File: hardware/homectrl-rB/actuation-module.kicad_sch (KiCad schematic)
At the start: 26 parts, among them J6 PUMP0-CONN, J7 PUMP1-CONN, J8 STEP-CONN, Q2 AO3400A, Q3 AO3400A, U8 TMC2209

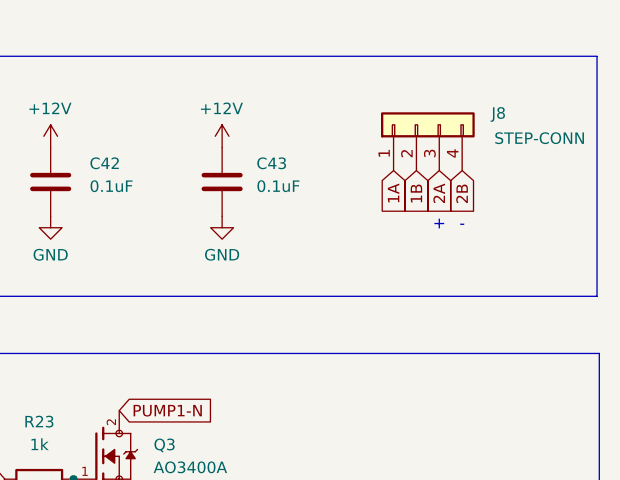
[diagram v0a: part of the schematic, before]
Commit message: connector fixes
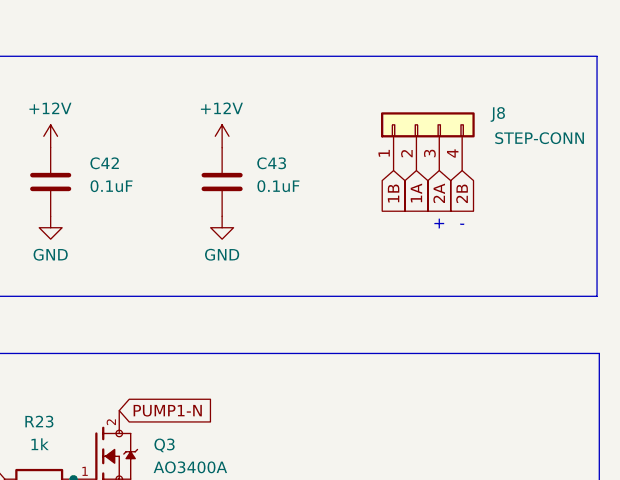
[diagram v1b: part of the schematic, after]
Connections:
- net 1A: now also J8.2 (Pin_2); no longer J8.1 (Pin_1)
- net 1B: now also J8.1 (Pin_1); no longer J8.2 (Pin_2)
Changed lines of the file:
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@@
+		)
+	)
+	(global_label "PGATE-1"
+		(shape input)
+		(at 161.29 67.31 180)
+		(fields_autoplaced yes)
+		(effects
+			(font
+				(size 1.27 1.27)
+			)
+			(justify right)
+		)
+		(property "Intersheetrefs" "${INTERSHEET_REFS}"
+			(at 149.7777 67.31 0)
+			(effects
+				(font
+					(size 1.27 1.27)
+				)
+				(justify right)
+				(hide yes)
+			)
+		)
+	)
+	(global_label "1A"
+		(shape input)
+		(at 207.01 33.02 270)
+		(fields_autoplaced yes)
+		(effects
+			(font
+				(size 1.27 1.27)
+			)
+			(justify right)
+		)
+		(property "Intersheetrefs" "${INTERSHEET_REFS}"
+			(at 207.01 38.3033 90)
+			(effects
+				(font
+					(size 1.27 1.27)
+				)
+				(justify right)
+				(hide yes)
+			)
+		)
+	)
+	(global_label "2B"
+		(shape input)
+		(at 118.11 105.41 90)
+		(fields_autoplaced yes)
+		(effects
+			(font
+				(size 1.27 1.27)
+			)
+			(justify left)
+		)
+		(property "Intersheetrefs" "${INTERSHEET_REFS}"
+			(at 118.11 99.9453 90)
+			(effects
+				(font
+					(size 1.27 1.27)
+				)
+				(justify left)
+				(hide yes)
+			)
+		)
+	)
+	(global_label "2A"
+		(shape input)
+		(at 209.55 33.02 270)
+		(fields_autoplaced yes)
+		(effects
+			(font
+				(size 1.27 1.27)
+			)
+			(justify right)
+		)
+		(property "Intersheetrefs" "${INTERSHEET_REFS}"
+			(at 209.55 38.3033 90)
+			(effects
+				(font
+					(size 1.27 1.27)
+				)
+				(justify right)
+				(hide yes)
+			)
+		)
+	)
+	(global_label "PUMP0-N"
+		(shape input)
+		(at 129.54 59.69 0)
+		(fields_autoplaced yes)
+		(effects
+			(font
+				(size 1.27 1.27)
+			)
+			(justify left)
+		)
+		(property "Intersheetrefs" "${INTERSHEET_REFS}"
+			(at 141.9595 59.69 0)
+			(effects
+				(font
+					(size 1.27 1.27)
+				)
+				(justify left)
+				(hide yes)
+			)
+		)
+	)
+	(global_label "S3-TX"
+		(shape input)
+		(at 118.11 146.05 270)
+		(fields_autoplaced yes)
+		(effects
+			(font
+				(size 1.27 1.27)
+			)
+			(justify right)
+		)
+		(property "Intersheetrefs" "${INTERSHEET_REFS}"
+			(at 118.11 155.2037 90)
+			(effects
+				(font
+					(size 1.27 1.27)
+				)
+				(justify right)
+				(hide yes)
+			)
+		)
+	)
+	(global_label "PUMP1-N"
+		(shape input)
+		(at 173.99 59.69 0)
+		(fields_autoplaced yes)
+		(effects
+			(font
+				(size 1.27 1.27)
+			)
+			(justify left)
+		)
+		(property "Intersheetrefs" "${INTERSHEET_REFS}"
+			(at 186.4095 59.69 0)
+			(effects
+				(font
+					(size 1.27 1.27)
+				)
+				(justify left)
+				(hide yes)
+			)
 		)
 	)
 	(global_label "1B"
 		(shape input)
-		(at 207.01 33.02 270)
-		(fields_autoplaced yes)
-		(effects
-			(font
-				(size 1.27 1.27)
-			)
-			(justify right)
-		)
-		(property "Intersheetrefs" "${INTERSHEET_REFS}"
-			(at 207.01 38.4847 90)
-			(effects
-				(font
-					(size 1.27 1.27)
-				)
-				(justify right)
-				(hide yes)
-			)
-		)
-	)
-	(global_label "PGATE-1"
-		(shape input)
-		(at 161.29 67.31 180)
-		(fields_autoplaced yes)
-		(effects
-			(font
-				(size 1.27 1.27)
-			)
-			(justify right)
-		)
-		(property "Intersheetrefs" "${INTERSHEET_REFS}"
-			(at 149.7777 67.31 0)
-			(effects
-				(font
-					(size 1.27 1.27)
-				)
-				(justify right)
-				(hide yes)
-			)
-		)
-	)
-	(global_label "2B"
-		(shape input)
-		(at 118.11 105.41 90)
-		(fields_autoplaced yes)
-		(effects
-			(font
-				(size 1.27 1.27)
-			)
-			(justify left)
-		)
-		(property "Intersheetrefs" "${INTERSHEET_REFS}"
-			(at 118.11 99.9453 90)
-			(effects
-				(font
-					(size 1.27 1.27)
-				)
-				(justify left)
-				(hide yes)
-			)
-		)
-	)
-	(global_label "2A"
-		(shape input)
-		(at 209.55 33.02 270)
-		(fields_autoplaced yes)
-		(effects
-			(font
-				(size 1.27 1.27)
-			)
-			(justify right)
-		)
-		(property "Intersheetrefs" "${INTERSHEET_REFS}"
-			(at 209.55 38.3033 90)
-			(effects
-				(font
-					(size 1.27 1.27)
-				)
-				(justify right)
-				(hide yes)
-			)
-		)
-	)
-	(global_label "PUMP0-N"
-		(shape input)
-		(at 129.54 59.69 0)
-		(fields_autoplaced yes)
-		(effects
-			(font
-				(size 1.27 1.27)
-			)
-			(justify left)
-		)
-		(property "Intersheetrefs" "${INTERSHEET_REFS}"
-			(at 141.9595 59.69 0)
-			(effects
-				(font
-					(size 1.27 1.27)
-				)
-				(justify left)
-				(hide yes)
-			)
-		)
-	)
-	(global_label "S3-TX"
-		(shape input)
-		(at 118.11 146.05 270)
-		(fields_autoplaced yes)
-		(effects
-			(font
-				(size 1.27 1.27)
-			)
-			(justify right)
-		)
-		(property "Intersheetrefs" "${INTERSHEET_REFS}"
-			(at 118.11 155.2037 90)
-			(effects
-				(font
-					(size 1.27 1.27)
-				)
-				(justify right)
-				(hide yes)
-			)
-		)
-	)
-	(global_label "PUMP1-N"
-		(shape input)
-		(at 173.99 59.69 0)
-		(fields_autoplaced yes)
-		(effects
-			(font
-				(size 1.27 1.27)
-			)
-			(justify left)
-		)
-		(property "Intersheetrefs" "${INTERSHEET_REFS}"
-			(at 186.4095 59.69 0)
+		(at 168.91 113.03 0)
+		(fields_autoplaced yes)
+		(effects
+			(font
+				(size 1.27 1.27)
+			)
+			(justify left)
+		)
+		(property "Intersheetrefs" "${INTERSHEET_REFS}"
+			(at 174.3747 113.03 0)
 			(effects
 				(font
@@
 	(global_label "1A"
 		(shape input)
+		(at 168.91 118.11 0)
+		(fields_autoplaced yes)
+		(effects
+			(font
+				(size 1.27 1.27)
+			)
+			(justify left)
+		)
+		(property "Intersheetrefs" "${INTERSHEET_REFS}"
+			(at 174.1933 118.11 0)
+			(effects
+				(font
+					(size 1.27 1.27)
+				)
+				(justify left)
+				(hide yes)
+			)
+		)
+	)
+	(global_label "1B"
+		(shape input)
 		(at 204.47 33.02 270)
 		(fields_autoplaced yes)
@@
 		)
 		(property "Intersheetrefs" "${INTERSHEET_REFS}"
-			(at 204.47 38.3033 90)
-			(effects
-				(font
-					(size 1.27 1.27)
-				)
-				(justify right)
-				(hide yes)
-			)
-		)
-	)
-	(global_label "1B"
-		(shape input)
-		(at 168.91 113.03 0)
-		(fields_autoplaced yes)
-		(effects
-			(font
-				(size 1.27 1.27)
-			)
-			(justify left)
-		)
-		(property "Intersheetrefs" "${INTERSHEET_REFS}"
-			(at 174.3747 113.03 0)
-			(effects
-				(font
-					(size 1.27 1.27)
-				)
-				(justify left)
-				(hide yes)
-			)
-		)
-	)
-	(global_label "1A"
-		(shape input)
-		(at 168.91 118.11 0)
-		(fields_autoplaced yes)
-		(effects
-			(font
-				(size 1.27 1.27)
-			)
-			(justify left)
-		)
-		(property "Intersheetrefs" "${INTERSHEET_REFS}"
-			(at 174.1933 118.11 0)
-			(effects
-				(font
-					(size 1.27 1.27)
-				)
-				(justify left)
-				(hide yes)
-			)
+			(at 204.47 38.4847 90)
+			(effects
+				(font
+					(size 1.27 1.27)
+				)
+				(justify right)
+				(hide yes)
+			)

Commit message: BOM fix
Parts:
- C27: value 2.2uF -> 2.2uF
- C29: value 22nF -> 22nF
- C30: value 4.7uF -> 4.7uF
- C33: value 220uF -> 220uF
- C41: value 100uF -> 100uF; Purchase (none) -> YES
- J6, J7: MPN N/A -> S02B-PASK-2; Purchase No -> Yes
- J8: MPN N/A -> S04B-PASK-2; Purchase No -> Yes
- Q2, Q3: Comments Confirmed AO3400A , brand:AOS,package:SOT-23-3L -> Confirmed AO3400A , brand:AOS,package:SOT-23-3L, and brand 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
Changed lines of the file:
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@@
 			)
 		)
-		(property "Comments" "Confirmed AO3400A  , brand:AOS,package:SOT-23-3L"
+		(property "Comments" "Confirmed AO3400A  , brand:AOS,package:SOT-23-3L, and brand AOS"
 			(at 127 64.77 0)
 			(effects
@@
 			)
 		)
-		(property "Value" "22nF "
+		(property "Value" "22nF"
 			(at 99.314 108.458 0)
 			(effects
@@
 			)
 		)
-		(property "Value" "2.2uF "
+		(property "Value" "2.2uF"
 			(at 85.598 127.508 0)
 			(effects
@@
 			)
 		)
-		(property "MPN" "N/A"
+		(property "MPN" "  S02B-PASK-2"
 			(at 118.11 27.94 0)
 			(effects
@@
 			)
 		)
-		(property "Purchase" "No"
+		(property "Purchase" "Yes"
 			(at 118.11 27.94 0)
 			(effects
@@
 			)
 		)
-		(property "MPN" "N/A"
+		(property "MPN" "  S04B-PASK-2"
 			(at 207.01 27.94 0)
 			(effects
@@
 			)
 		)
-		(property "Purchase" "No"
+		(property "Purchase" "Yes"
 			(at 207.01 27.94 0)
 			(effects
@@
 			)
 		)
-		(property "Comments" "Confirmed AO3400A  , brand:AOS,package:SOT-23-3L"
+		(property "Comments" "Confirmed AO3400A  , brand:AOS,package:SOT-23-3L, and brand AOS"
 			(at 171.45 64.77 0)
 			(effects
@@
 			)
 		)
-		(property "Value" "100uF "
+		(property "Value" "100uF"
 			(at 151.13 34.6709 0)
 			(effects
@@
 			)
 		)
+		(property "Purchase" "YES"
+			(at 147.32 34.29 0)
+			(effects
+				(font
+					(size 1.27 1.27)
+				)
+				(hide yes)
+			)
+		)
 		(pin "2"
 		)
@@
 			)
 		)
-		(property "Value" "220uF "
+		(property "Value" "220uF"
 			(at 215.392 116.332 0)
 			(effects
@@
 			)
 		)
-		(property "MPN" "N/A"
+		(property "MPN" "  S02B-PASK-2"
 			(at 86.36 27.94 0)
 			(effects
@@
 			)
 		)
-		(property "Purchase" "No"
+		(property "Purchase" "Yes"
 			(at 86.36 27.94 0)
 			(effects
@@
 			)
 		)
-		(property "Value" "4.7uF "
+		(property "Value" "4.7uF"
 			(at 85.344 132.842 0)
 			(effects
